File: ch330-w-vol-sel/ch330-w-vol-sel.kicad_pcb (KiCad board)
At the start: 2 copper layers, 17.1 x 20.3 mm, 14 parts, among them J1 USB_A, J2 Conn_01x04, J3 Conn_01x03, U1 CH330N, U2 LM1117-3.3

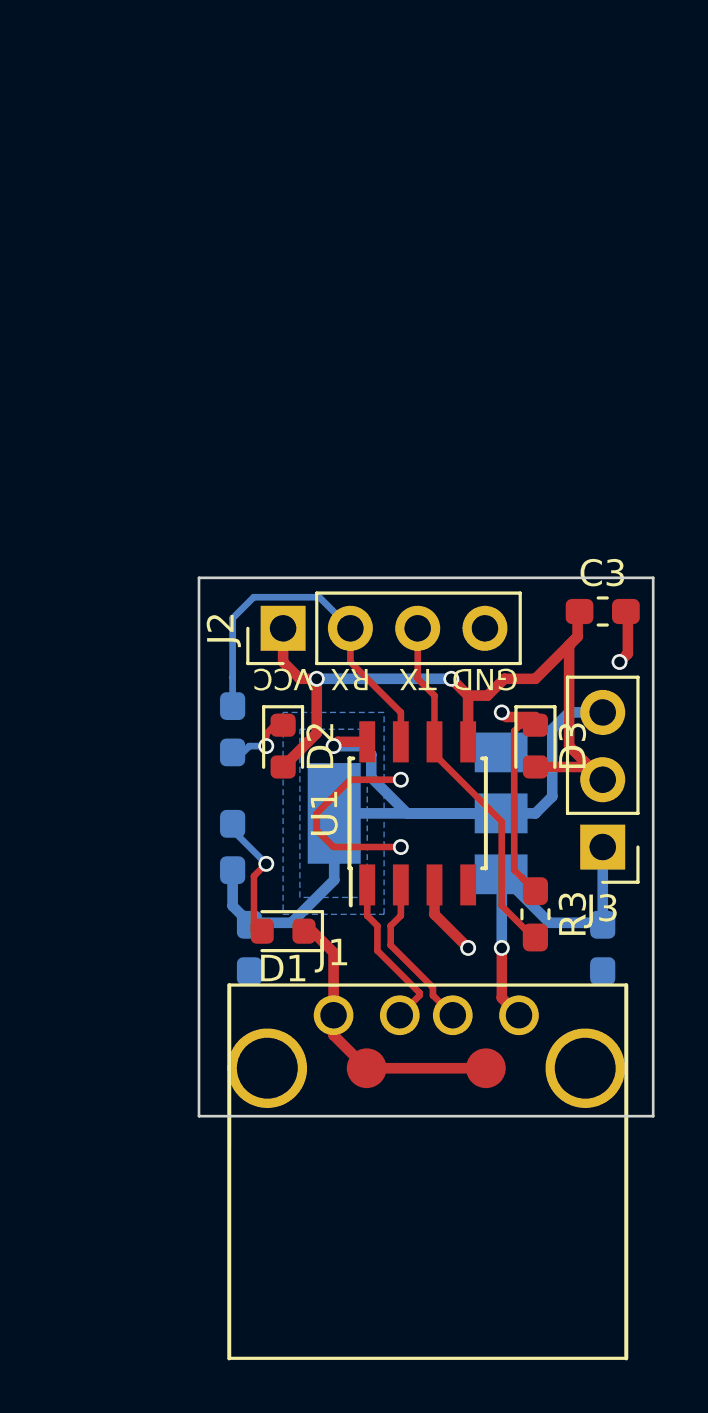
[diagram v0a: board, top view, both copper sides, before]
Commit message: update new ch330 designs
Signed-off-by: Icenowy Zheng <icenowy@aosc.io>
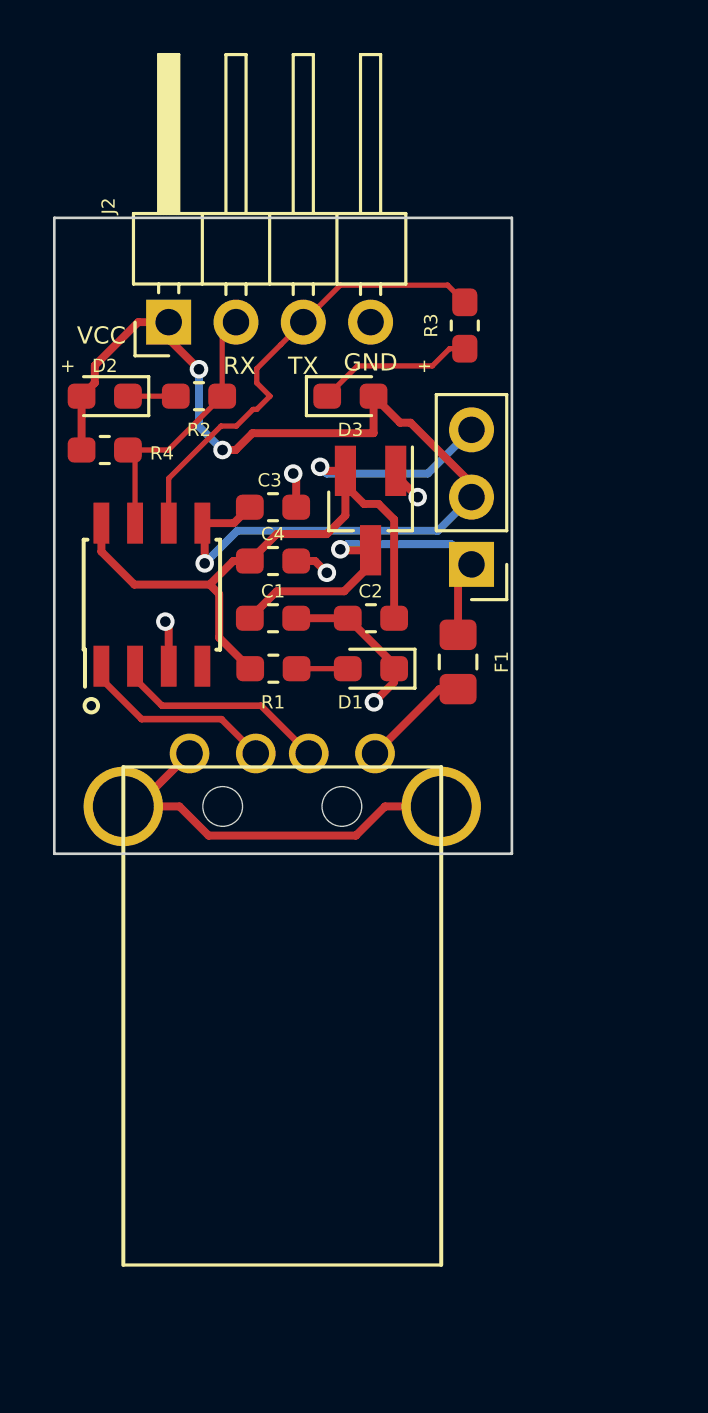
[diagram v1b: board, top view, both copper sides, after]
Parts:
- added C4: 0.1uF, Capacitor_SMD:C_0603_1608Metric_Pad1.05x0.95mm_HandSolder, F.Cu at (145.7, 88.9)
- added F1: >5.2V 100mA, Resistor_SMD:R_0805_2012Metric_Pad1.15x1.40mm_HandSolder, F.Cu at (152.7, 92.7)
- added R4: 10kR, Resistor_SMD:R_0603_1608Metric_Pad1.05x0.95mm_HandSolder, F.Cu at (139.3, 84.7)
- C1, C2: value 10μF -> 1uF; moved to F.Cu
- C3: value 0.1μF -> 0.1uF
- D1, D2, D3: footprint LED_SMD:LED_0603_1608Metric_Pad0.88x0.95mm_HandSolder -> LED_SMD:LED_0603_1608Metric_Pad1.05x0.95mm_HandSolder
- J2: value Conn_01x04 -> UART; footprint Connector_PinHeader_2.54mm:PinHeader_1x04_P2.54mm_Vertical -> Connector_PinHeader_2.54mm:PinHeader_1x04_P2.54mm_Horizontal
- J3: value Conn_01x03 -> VOL SEL
- R1, R2: value 120R -> 1.5kR; moved to F.Cu
- R3: value 120R -> 1.5kR
- U2: value LM1117-3.3 -> XC6206P33; footprint Package_TO_SOT_SMD:SOT-223-3_TabPin2 -> Package_TO_SOT_SMD:SOT-23_Handsoldering; moved to F.Cu
- moved R3 22.4 mm to (152.9, 80.0), turned to 90 degrees
- moved C1 17.6 mm to (145.7, 91.1), turned to 0 degrees
- moved D3 14.9 mm to (148.6, 82.7), turned to 0 degrees
- moved D2 14.8 mm to (139.3, 82.7), turned to 180 degrees
- moved C2 13.3 mm to (149.4, 91.1), turned to 180 degrees
- moved C3 13.1 mm to (145.7, 86.9)
- moved U1 13.0 mm to (141.1, 90.2)
- moved R2 12.6 mm to (142.9, 82.7), turned to 180 degrees
- moved J2 12.3 mm to (141.7, 79.9)
- moved J3 11.8 mm to (153.2, 89.0)
- moved U2 11.6 mm to (149.4, 87.0), turned to 270 degrees
- moved J1 11.3 mm to (142.5, 96.2)
- moved D1 10.4 mm to (149.4, 93.0)
- moved R1 6.90 mm to (145.7, 93.0), turned to 180 degrees
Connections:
- net Net-(J2-Pad2) renamed /RX
- net Net-(J2-Pad3) renamed /TX
- J1 pad 1: VBUS -> Net-(F1-Pad2)
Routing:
- net VCC: track 29.2 -> 39.9 mm, vias 2 -> 3
- net GND: track 23.2 -> 28.1 mm, vias 4 -> 5
- net Net-(F1-Pad2): track 0.00 -> 4.14 mm
- net /TX: track 13.7 -> 17.5 mm
- net /RX: track 13.4 -> 10.3 mm
- net Net-(D1-Pad2): track 4.99 -> 1.93 mm, vias 1 -> 0
- net Net-(D3-Pad1): track 8.60 -> 5.94 mm, vias 1 -> 0
- net /D-: track 6.05 -> 8.20 mm
- net /D+: track 6.05 -> 7.47 mm
- net VBUS: track 14.0 -> 15.3 mm
- net Net-(D2-Pad1): track 2.83 -> 1.81 mm, vias 1 -> 0
- net +3V3: track 30.8 -> 31.5 mm
- removed copper zone on B.Cu, net +3V3
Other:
- board size 17.1 x 20.3 mm -> 17.3 x 24 mm
- net class Default: trace_width 0.25 -> 0.2; via_drill 0.4 -> 0.3
- net class Power: trace_width 0.4 -> 0.3; via_dia 0.6 -> 0.7
- rule pad_to_mask_clearance: 0 -> 0.2
- rule trace_min: 0.2 -> 0.16
- rule via_min_size: 0.4 -> 0.6
- board text added: "+"
- board text added: "CH330N USB2TTL"
- board text added: "by Icenowy"
- board text removed: "--Icenowy"
- board text removed: "3V3"
- board text removed: "5V"
- board text removed: "Simple USB2TTL"

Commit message: ch330-w-vol-sel: fixes
Signed-off-by: Icenowy Zheng <icenowy@aosc.io>
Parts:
- R4: value 10kR -> 4.7kR
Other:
- board text added: "3V3"
- board text added: "5V"
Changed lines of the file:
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@@
   (general
     (thickness 1)
-    (drawings 17)
+    (drawings 19)
     (tracks 124)
     (zones 0)
@@
       (effects (font (size 0.5 0.5) (thickness 0.125)))
     )
-    (fp_text value 10kR (at 0 1.43) (layer F.Fab)
+    (fp_text value 4.7kR (at 0 1.43) (layer F.Fab)
       (effects (font (size 1 1) (thickness 0.15)))
     )
@@
     )
   )
+  (gr_text 3V3 (at 150.622 84.074) (layer B.SilkS)
+    (effects (font (size 0.85 0.85) (thickness 0.2125)) (justify mirror))
+  )
+  (gr_text 5V (at 150.876 89.281) (layer B.SilkS)
+    (effects (font (size 0.85 0.85) (thickness 0.2125)) (justify mirror))
+  )
   (gr_text GND (at 149.352 81.407) (layer F.SilkS)
